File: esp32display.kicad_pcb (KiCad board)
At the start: 4 copper layers, 85 x 50 mm, 32 parts, among them J1 V_IN, J2 V_PANEL, J3 USB-C Power Only, J4 LIS3DH, J5 RGB_PANEL, J6 TOUCH, J7 NPX1, J8 NPX2, J9 PROG, SW1 SW_Push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

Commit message: Submitted V0.2 to production
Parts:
- removed C3: 10u, Capacitor_SMD:C_1206_3216Metric
- removed D2, D3: WS2812B, LED_SMD:LED_WS2812B_PLCC4_5.0x5.0mm_P3.2mm
- removed J1: V_IN, Power_Pads:2 x 0.2 Pads
- removed the J4 at (148.3, 121.0)
- removed J8: NPX2, Connector_PinHeader_2.54mm:PinHeader_1x03_P2.54mm_Vertical
- removed the R5 at (137.0, 111.0)
- removed REF** (x4): MountingHole_3.2mm_M3_Pad_Via, MountingHole:MountingHole_3.2mm_M3_Pad_Via
- removed SW3: BOOT, Button_Switch_SMD:SW_Push_1P1T_NO_CK_KSC7xxJ
- added R6: 10k, Resistor_SMD:R_0603_1608Metric_Pad0.98x0.95mm_HandSolder, F.Cu at (147.0, 118.0)
- added U2: LIS3DH, Package_LGA:LGA-16_3x3mm_P0.5mm_LayoutBorder3x5y, F.Cu at (153.5, 121.0)
- J2: footprint Power_Pads:2 x 0.2 Pads -> Connector_PinHeader_2.54mm:PinHeader_1x02_P2.54mm_Vertical
- J3: value USB-C Power Only -> USB_C_Receptacle_PowerOnly_6P; footprint usb-c_recepticle_LCSC-C165948_hand_solder:USB-C_LCSC_C165948_Hand_Solder -> Connector_USB:USB_C_Receptacle_GCT_USB4125-xx-x_6P_TopMnt_Horizontal
- J5: renamed from J6; footprint Connector_PinHeader_2.54mm:PinHeader_1x02_P2.54mm_Vertical -> Connector_JST:JST_PH_S2B-PH-K_1x02_P2.00mm_Horizontal
- J6: renamed from J7; footprint Connector_PinHeader_2.54mm:PinHeader_1x03_P2.54mm_Vertical -> Connector_JST:JST_PH_S3B-PH-K_1x03_P2.00mm_Horizontal
- R4: footprint OptoDevice:R_LDR_5.1x4.3mm_P3.4mm_Vertical -> Connector_JST:JST_PH_S2B-PH-K_1x02_P2.00mm_Horizontal
- SW1: value SW_Push -> Reset; footprint Button_Switch_SMD:SW_Push_1P1T_NO_CK_KSC7xxJ -> Button_Switch_SMD:SW_Push_1P1T_XKB_TS-1187A
- SW2: value RESET -> Boot; footprint Button_Switch_SMD:SW_Push_1P1T_NO_CK_KSC7xxJ -> Button_Switch_SMD:SW_Push_1P1T_XKB_TS-1187A
- U1: value AMS1117-3.3 -> LD1117S12TR_SOT223
- U3: renamed from U2; footprint RF_Module:ESP32-WROOM-32 -> RF_Module:ESP32-WROOM-32D
- moved J7 63.2 mm to (136.3, 121.0)
- moved J3 56.5 mm to (163.7, 130.0), turned to 0 degrees
- moved R1 39.9 mm to (168.5, 123.5)
- moved R2 37.6 mm to (166.5, 123.5), turned to -90 degrees
- moved J2 36.8 mm to (167.7, 103.7), turned to 0 degrees
- moved SW2 35.8 mm to (149.5, 114.0), turned to 0 degrees
- moved J4 35.0 mm to (159.2, 101.5)
- moved D1 32.3 mm to (167.7, 118.0)
- moved C5 31.6 mm to (139.8, 118.0), turned to 180 degrees
- moved J6 29.9 mm to (151.2, 127.0), turned to 0 degrees
- moved R5 29.7 mm to (143.4, 118.0), turned to 0 degrees
- moved J5 26.7 mm to (143.7, 127.0), turned to 0 degrees
- moved C1 25.0 mm to (157.5, 94.0), turned to 180 degrees
- moved C2 24.9 mm to (157.5, 89.5), turned to 180 degrees
- moved C4 20.6 mm to (157.5, 91.5), turned to 180 degrees
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- renumbered J5 to J4, J9 to J7, R6 to R5
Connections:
- D1 pad 2: Net-(D1-Pad2) -> VBUS
- J2 pad 2: +5V -> VBUS
- J3 pad A9: Net-(D1-Pad2) -> VBUS
- J3 pad B9: Net-(D1-Pad2) -> VBUS
- J6 pad 1: +5V -> VBUS
- J6 pad 2: Net-(D2-Pad2) -> NPX1
- SW1 pad 2: BUTTON -> RESET
- SW2 pad 2: RESET -> BOOT
- U3 pad 37: NPX2 -> INT1
- U3 pad 6: BUTTON -> INT2
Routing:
- net INT2: track 0.00 -> 76.8 mm, vias 0 -> 2
- net VBUS: track 0.00 -> 55.2 mm
- net INT1: track 0.00 -> 54.4 mm, vias 0 -> 2
- net NPX2: track 41.7 -> 0.00 mm, vias 2 -> 0
- net BUTTON: track 35.9 -> 0.00 mm, vias 2 -> 0
- net C: track 48.7 -> 20.3 mm
- net OE: track 25.1 -> 53.2 mm, vias 1 -> 2
- net BOOT: track 57.8 -> 29.9 mm
- net Net-(D1-Pad2): track 27.1 -> 0.00 mm, vias 2 -> 0
- net LAT: track 21.8 -> 48.8 mm, vias 1 -> 2
- net D: track 44.5 -> 17.9 mm
- net A: track 40.4 -> 13.7 mm, vias 0 -> 1
- net B: track 45.1 -> 18.9 mm
- net CLK: track 57.0 -> 31.7 mm, vias 1 -> 2
- net +5V: track 27.9 -> 6.59 mm, vias 1 -> 2
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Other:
- board size 85 x 50 mm -> 36 x 45.6 mm
- board text added: "ESP can be programmed using this header. NeoPixels and RGB panel will only work if the USB-C is connected and supplying power"
- board text added: "LDR"
- board text added: "NPX"
- board text added: "RGB Panel Driver"
- board text added: "TOUCH"
- board text added: "V0.2"
- board text added: "⏚"
- board text removed: "PRESS"
- board text removed: "SCL"
- board text removed: "SDA"
- board text removed: "TOUCH1"
- board text removed: "TOUCH2"
- board text removed: "V0.1"
- board text removed: "X"

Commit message: Added I2C Pullup Resistors
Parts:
- added R7: 4K7, Resistor_SMD:R_0603_1608Metric_Pad0.98x0.95mm_HandSolder, F.Cu at (167.5, 97.0)
- added R8: 4K7, Resistor_SMD:R_0603_1608Metric_Pad0.98x0.95mm_HandSolder, F.Cu at (167.5, 98.5)
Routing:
- net SDA: track 29.3 -> 42.9 mm, vias 0 -> 2
- net SCL: track 31.8 -> 41.7 mm
- net +3V3: track 26.2 -> 32.8 mm
- net +5V: track 6.59 -> 5.79 mm

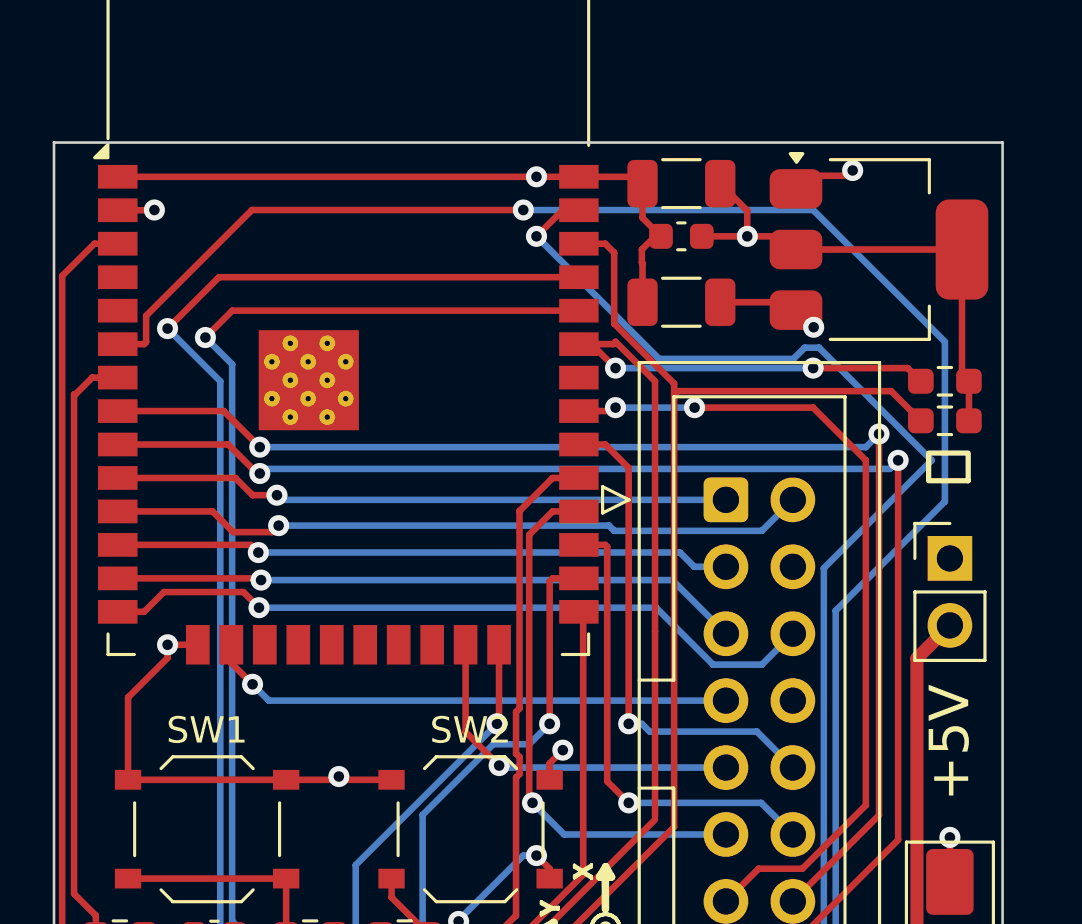
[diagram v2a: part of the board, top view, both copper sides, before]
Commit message: Minor fixes from V0.2.  Corrected C1 & C2 package sizes.  Improved pushbutton marking on silkscreen.
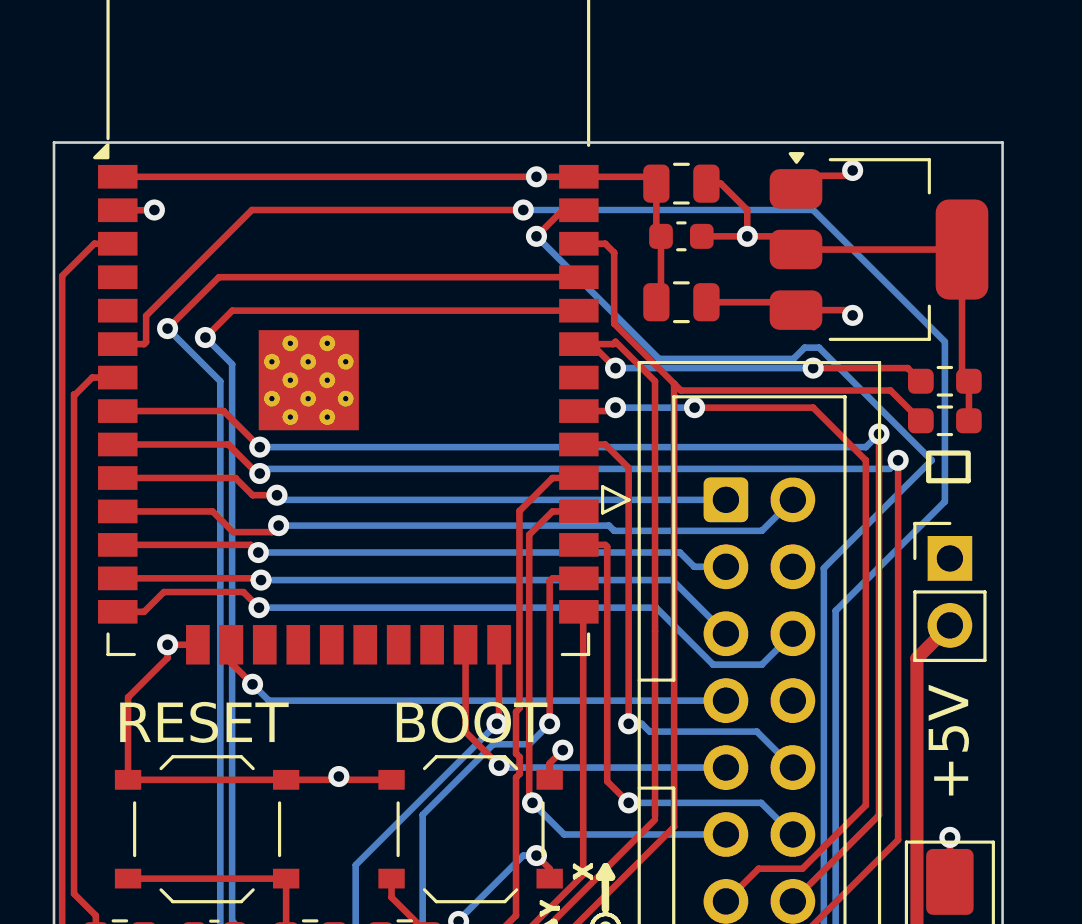
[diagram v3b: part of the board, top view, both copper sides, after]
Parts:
- C1, C2: footprint Capacitor_SMD:C_1206_3216Metric -> Capacitor_SMD:C_0805_2012Metric
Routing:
- net +5V: track 5.79 -> 8.88 mm
- net +3V3: track 32.8 -> 33.4 mm
